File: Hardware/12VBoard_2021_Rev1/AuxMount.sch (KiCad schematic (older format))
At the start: 35 parts, among them Q4 CSD18537NQ5A, Q5 CSD18531Q5A, U10 LM5116, U11 INA198, U17 LM2576S-12/NOPB

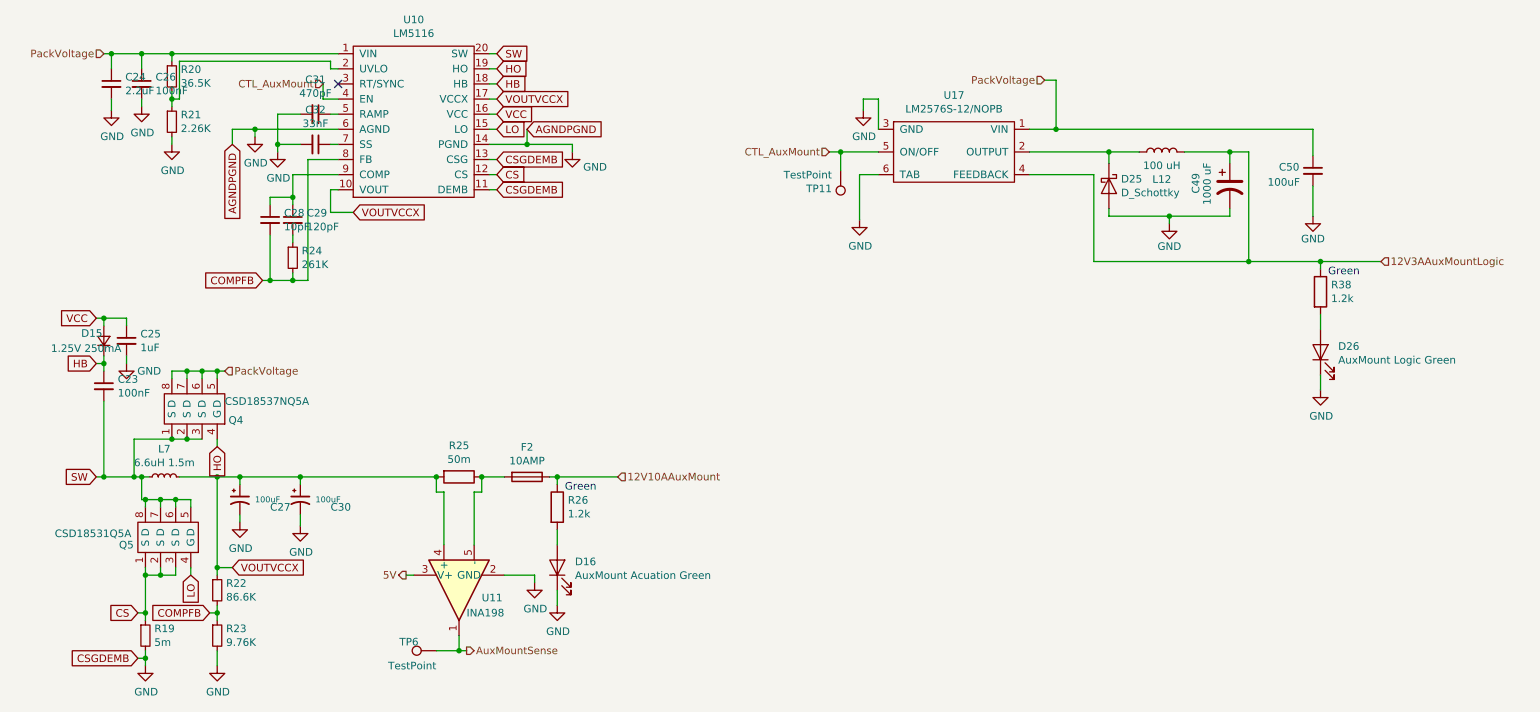
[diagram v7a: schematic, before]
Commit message: Changes!
Added the new correct connectors and redid all signal lines to the High Current side of the board. Also deleted all uncessacary components on the High current side that are no longer used.
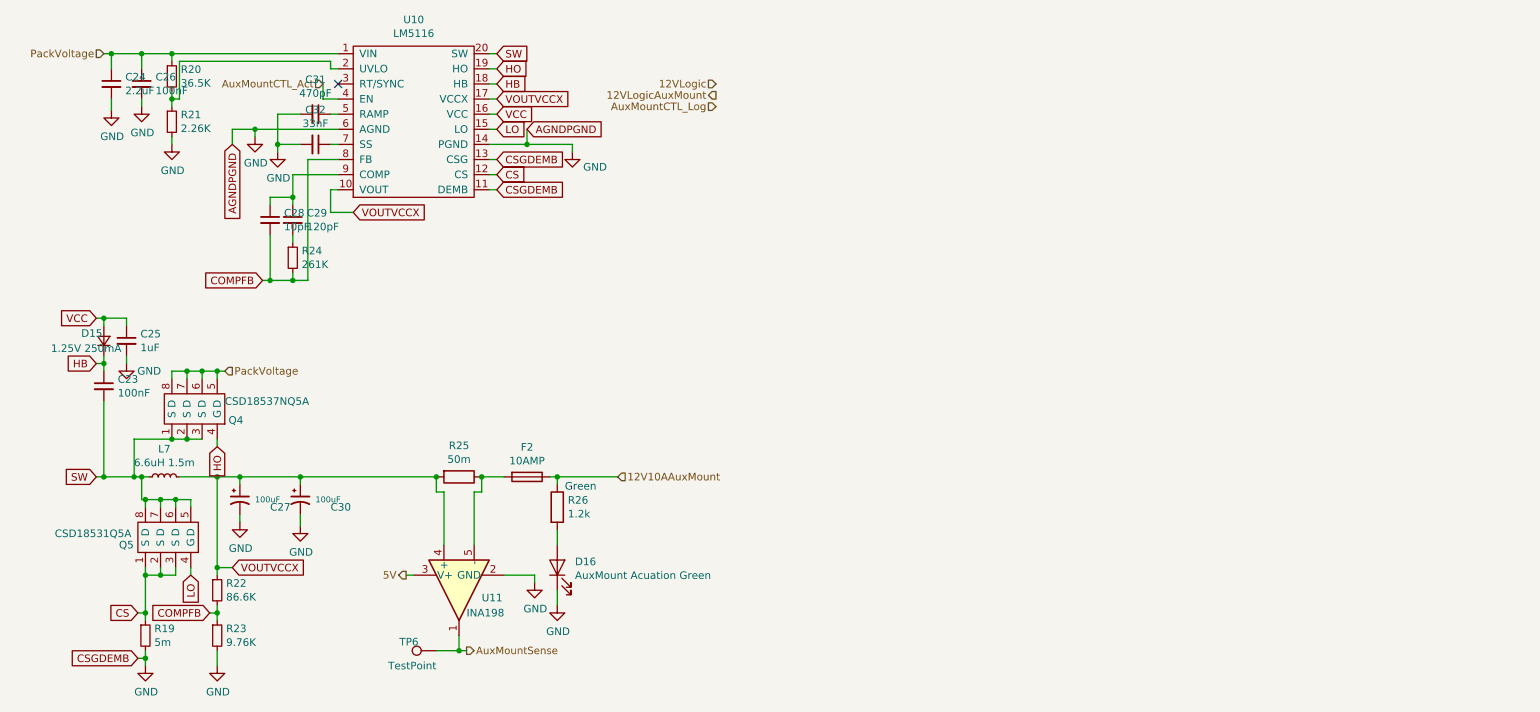
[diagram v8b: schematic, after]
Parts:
- removed C49: 1000 uF, Capacitor_THT:CP_Radial_D10.0mm_P5.00mm, symbol Device:CP1
- removed C50: 100uF, Capacitor_SMD:C_0603_1608Metric_Pad1.05x0.95mm_HandSolder, symbol Device:C_Small
- removed D25: D_Schottky, Diode_THT:D_DO-201AD_P5.08mm_Vertical_KathodeUp, symbol Device:D_Schottky
- removed D26: AuxMount Logic Green, Diode_SMD:D_0603_1608Metric_Pad1.05x0.95mm_HandSolder, symbol Device:LED
- removed L12: 100 uH, Inductor_SMD:L_0603_1608Metric_Pad1.05x0.95mm_HandSolder, symbol Device:L
- removed R38: 1.2k, Resistor_SMD:R_0603_1608Metric_Pad1.05x0.95mm_HandSolder, symbol Device:R
- removed TP11: TestPoint, TestPoint:TestPoint_Pad_2.5x2.5mm, symbol Connector:TestPoint
- removed U17: LM2576S-12/NOPB, MRDT_Devices:LM2576, symbol 12VBoard_2021_Rev1-rescue:LM2576D2TR4-MRDT_Devices
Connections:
- net CTL_AuxMount renamed AuxMountCTL_Act
